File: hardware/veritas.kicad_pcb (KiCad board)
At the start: 2 copper layers, 43 parts, among them J1 ~{USB_BOOT}, J2 USB_C_Receptacle_USB2.0, J3 VIDEO, J4 VIDEO, J5 SYNC, J6 CONTROLLER_PORT, J7 CON_RESET, Q1 LMBT3946DW1T1G, U1 W25Q128JVSIQ, U2 NCP1117ST33T3G, U3 RP2040, U4 LM1881, Y1 12MHz

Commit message: Finished first hardware prototype.
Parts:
- added C17: 0.1uF, Capacitor_SMD:C_0603_1608Metric_Pad1.08x0.95mm_HandSolder, F.Cu at (154.7, 79.9)
- added C19: 0.1uF, Capacitor_SMD:C_0603_1608Metric_Pad1.08x0.95mm_HandSolder, F.Cu at (141.9, 111.8)
- added C22: 0.1uF, Capacitor_SMD:C_0603_1608Metric_Pad1.08x0.95mm_HandSolder, F.Cu at (170.2, 120.1)
- added C23: 0.1uF, Capacitor_SMD:C_0603_1608Metric_Pad1.08x0.95mm_HandSolder, F.Cu at (153.4, 115.2)
- added J11: DEBUG, Connector_PinHeader_2.54mm:PinHeader_1x06_P2.54mm_Horizontal, F.Cu at (174.4, 120.9)
- added J2: DISPLAY0, Connector_PinHeader_2.54mm:PinHeader_1x05_P2.54mm_Horizontal, F.Cu at (156.3, 70.1)
- added J3: DISPLAY1, Connector_PinHeader_2.54mm:PinHeader_1x05_P2.54mm_Horizontal, F.Cu at (141.9, 70.1)
- added J4: DISPLAY2, Connector_PinHeader_2.54mm:PinHeader_1x05_P2.54mm_Horizontal, F.Cu at (127.4, 70.1)
- added J5: DISPLAY3, Connector_PinHeader_2.54mm:PinHeader_1x05_P2.54mm_Horizontal, F.Cu at (112.9, 70.1)
- added JP3: DJ-, Jumper:SolderJumper-3_P1.3mm_Open_RoundedPad1.0x1.5mm_NumberLabels, F.Cu at (173.9, 103.2)
- added JP4: DJ+, Jumper:SolderJumper-3_P1.3mm_Open_RoundedPad1.0x1.5mm_NumberLabels, F.Cu at (173.9, 98.4)
- added JP5: SolderJumper_2_Open, Jumper:SolderJumper-2_P1.3mm_Open_TrianglePad1.0x1.5mm, B.Cu at (162.0, 111.9)
- added JP6: SolderJumper_2_Open, Jumper:SolderJumper-2_P1.3mm_Open_TrianglePad1.0x1.5mm, B.Cu at (162.0, 109.7)
- added JP7: SolderJumper_2_Open, Jumper:SolderJumper-2_P1.3mm_Open_TrianglePad1.0x1.5mm, B.Cu at (177.2, 120.2)
- added Q2: 2N7002K, Package_TO_SOT_SMD:SOT-23_Handsoldering, F.Cu at (124.7, 121.5)
- added R10: 10K, Resistor_SMD:R_0603_1608Metric_Pad0.98x0.95mm_HandSolder, F.Cu at (124.7, 117.9)
- added R12: 10K, Resistor_SMD:R_0603_1608Metric_Pad0.98x0.95mm_HandSolder, F.Cu at (123.8, 125.1)
- added R3: 1K, Resistor_SMD:R_0603_1608Metric_Pad0.98x0.95mm_HandSolder, F.Cu at (132.5, 93.3)
- added REF**: JLC_ToolingHole, veritas:JLC_ToolingHole, F.Cu at (183.1, 61.3)
- added REF**: JLC_ToolingHole, veritas:JLC_ToolingHole, F.Cu at (111.1, 63.2)
- added REF**: JLC_ToolingHole, veritas:JLC_ToolingHole, F.Cu at (113.0, 133.1)
- added SW1: ~{BOOT_SEL}, Button_Switch_SMD:SW_SPST_PTS645, F.Cu at (179.6, 86.1)
- added U4: MCP2221A, Package_DIP:DIP-14_W7.62mm, F.Cu at (157.1, 80.5)
- added U6: TXS0108EPW, Package_SO:TSSOP-20_4.4x6.5mm_P0.65mm, F.Cu at (159.0, 113.4)
- added U7: TXS0108EPW, Package_SO:TSSOP-20_4.4x6.5mm_P0.65mm, F.Cu at (147.6, 113.4)
- added U8: TXS0108EPW, Package_SO:TSSOP-20_4.4x6.5mm_P0.65mm, F.Cu at (136.1, 113.4)
- J1: value ~{USB_BOOT} -> DISPLAY_PWR; footprint Connector_PinHeader_2.54mm:PinHeader_1x02_P2.54mm_Vertical -> Connector_BarrelJack:BarrelJack_Horizontal
- J7: renamed from J2; value USB_C_Receptacle_USB2.0 -> USB2.0_C; footprint veritas:2171790001 -> veritas:TYPE-C-31-M-12
- Q1: footprint Package_TO_SOT_SMD:SOT-363_SC-70-6 -> Package_TO_SOT_SMD:SOT-363_SC-70-6_Handsoldering
- moved C2 74.6 mm to (131.7, 96.5), turned to 180 degrees
- moved J7 63.2 mm to (183.0, 100.8), turned to 90 degrees
- moved C7 62.8 mm to (172.7, 117.9)
- moved J1 61.7 mm to (171.8, 67.4), turned to 180 degrees
- moved R9 61.5 mm to (180.2, 94.7), turned to 0 degrees
- moved C4 59.8 mm to (146.4, 97.5)
- moved R8 59.6 mm to (180.2, 107.0), turned to 0 degrees
- moved C5 56.6 mm to (137.8, 100.7), turned to -90 degrees
- moved JP1 55.9 mm to (127.9, 81.2)
- moved R4 55.9 mm to (127.9, 79.2)
- moved C1 54.2 mm to (131.7, 95.0), turned to 180 degrees
- moved R5 52.8 mm to (124.5, 79.2), turned to 0 degrees
- moved C12 50.7 mm to (138.3, 86.4), turned to 90 degrees
- moved C3 50.5 mm to (142.6, 99.0), turned to -90 degrees
- moved C6 49.4 mm to (146.4, 99.1)
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- renumbered C17 to C18, C18 to C20, C19 to C21, J5 to J10, J6 to J12, J7 to J6, J3 to J8, J4 to J9, R9 to R11, R7 to R4, R8 to R5, R3 to R6, R6 to R7, R4 to R8, R5 to R9, U4 to U5
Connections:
- net ALT_CLK renamed ALT_CLK_B
- J1 pad 1: Net-(J1-Pad1) -> /LED_5V
- J12 pad 1: unconnected-(J6-Pad1) -> CP_1
- J12 pad 10: VBUS -> +3V3
- J12 pad 11: unconnected-(J6-Pad11) -> CP_11
- J12 pad 12: unconnected-(J6-Pad12) -> CP_12
- J12 pad 13: unconnected-(J6-Pad13) -> CP_13
- J12 pad 14: unconnected-(J6-Pad14) -> CP_14
- J12 pad 15: unconnected-(J6-Pad15) -> CP_15
- J12 pad 16: unconnected-(J6-Pad16) -> CP_16
- J12 pad 17: unconnected-(J6-Pad17) -> CP_17
- J12 pad 18: unconnected-(J6-Pad18) -> CP_18
- J12 pad 19: +3V3 -> VBUS
- J12 pad 2: unconnected-(J6-Pad2) -> CP_2
- J12 pad 20: unconnected-(J6-Pad20) -> CP_20
- J12 pad 21: unconnected-(J6-Pad21) -> CP_21
- J12 pad 22: unconnected-(J6-Pad22) -> CP_22
- J12 pad 23: unconnected-(J6-Pad23) -> CP_23
- J12 pad 24: unconnected-(J6-Pad24) -> CP_24
- J12 pad 25: unconnected-(J6-Pad25) -> CP_25
- J12 pad 3: unconnected-(J6-Pad3) -> CP_3
- J12 pad 4: unconnected-(J6-Pad4) -> CP_4
- J12 pad 5: unconnected-(J6-Pad5) -> CP_5
- J12 pad 6: unconnected-(J6-Pad6) -> CP_6
- J12 pad 7: unconnected-(J6-Pad7) -> CP_7
- J12 pad 8: unconnected-(J6-Pad8) -> CP_8
- J6 pad 2: /RESET_HI -> /RESET_LO
- J6 pad 3: /RESET_LO -> /RESET_HI
- J7 pad A6: /D+ -> /PORTD+
- J7 pad A7: /D- -> /PORTD-
- J7 pad B6: /D+ -> /PORTD+
- J7 pad B7: /D- -> /PORTD-
- Q1 pad 6: VDD -> CP_20
- R1 pad 1: Net-(J1-Pad1) -> Net-(R1-Pad1)
- U3 pad 11: unconnected-(U3-Pad11) -> BRIDGE_RX
- U3 pad 12: unconnected-(U3-Pad12) -> BRIDGE_TX
- U3 pad 13: unconnected-(U3-Pad13) -> CON_RESET
- U3 pad 14: unconnected-(U3-Pad14) -> ALT_CLK_A
- U3 pad 15: unconnected-(U3-Pad15) -> CNT_0
- U3 pad 16: unconnected-(U3-Pad16) -> CNT_1
- U3 pad 17: unconnected-(U3-Pad17) -> CNT_2
- U3 pad 18: unconnected-(U3-Pad18) -> CNT_3
- U3 pad 19: unconnected-(U3-Pad19) -> GND
- U3 pad 2: unconnected-(U3-Pad2) -> CNT_17
- U3 pad 21: Net-(C14-Pad2) -> Net-(R3-Pad2)
- U3 pad 24: unconnected-(U3-Pad24) -> SWCLK
- U3 pad 25: unconnected-(U3-Pad25) -> SWD
- U3 pad 26: unconnected-(U3-Pad26) -> +3V3
- U3 pad 27: unconnected-(U3-Pad27) -> CNT_4
- U3 pad 28: unconnected-(U3-Pad28) -> CNT_5
- U3 pad 29: unconnected-(U3-Pad29) -> CNT_6
- U3 pad 3: unconnected-(U3-Pad3) -> CNT_18
- U3 pad 30: unconnected-(U3-Pad30) -> CNT_7
- U3 pad 31: unconnected-(U3-Pad31) -> CNT_8
- U3 pad 32: unconnected-(U3-Pad32) -> CNT_9
- U3 pad 34: unconnected-(U3-Pad34) -> CNT_10
- U3 pad 35: unconnected-(U3-Pad35) -> CNT_11
- U3 pad 36: unconnected-(U3-Pad36) -> CNT_12
- U3 pad 37: unconnected-(U3-Pad37) -> CNT_13
- U3 pad 38: unconnected-(U3-Pad38) -> CNT_14
- U3 pad 39: unconnected-(U3-Pad39) -> CNT_15
- U3 pad 4: unconnected-(U3-Pad4) -> DISPLAY_STROBE0
- U3 pad 40: unconnected-(U3-Pad40) -> CNT_16
- U3 pad 41: unconnected-(U3-Pad41) -> DETECT
- U3 pad 5: unconnected-(U3-Pad5) -> DISPLAY_STROBE1
- U3 pad 6: unconnected-(U3-Pad6) -> DISPLAY_STROBE2
- U3 pad 7: unconnected-(U3-Pad7) -> DISPLAY_STROBE3
- U3 pad 8: unconnected-(U3-Pad8) -> DISPLAY_SER
- U3 pad 9: unconnected-(U3-Pad9) -> DISPLAY_CLK
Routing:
- net +3V3: track 15.4 -> 225.7 mm, vias 0 -> 4
- net SWCLK: track 0.00 -> 132.0 mm, vias 0 -> 2
- net SWD: track 0.00 -> 129.2 mm, vias 0 -> 2
- net GND: track 16.1 -> 135.4 mm, vias 6 -> 28
- net DISPLAY_CLK: track 0.00 -> 116.8 mm
- net DISPLAY_SER: track 0.00 -> 111.7 mm, vias 0 -> 1
- net VBUS: track 2.54 -> 101.3 mm, vias 0 -> 3
- net CP_20: track 0.00 -> 97.9 mm, vias 0 -> 1
- net /LED_5V: track 0.00 -> 80.1 mm
- net CNT_17: track 0.00 -> 70.3 mm, vias 0 -> 3
- net CNT_18: track 0.00 -> 65.2 mm, vias 0 -> 3
- net ALT_CLK_A: track 0.00 -> 51.3 mm, vias 0 -> 2
- net DISPLAY_STROBE3: track 0.00 -> 40.0 mm
- net DISPLAY_STROBE0: track 0.00 -> 36.0 mm
- net Net-(R1-Pad1): track 0.00 -> 35.1 mm
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- added copper zone on F.Cu, net +1V1
- added copper zone on F.Cu, net +3V3
- added copper zone on B.Cu, net GND
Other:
- board outline added: 76.1 x 77.3 mm
- board text added: "5V"
- board text added: "ALT_CLK"
- board text added: "CVIN"
- board text added: "DEBUG_RX"
- board text added: "DEBUG_TX"
- board text added: "GND"
- board text added: "JLCJLCJLCJLC"
- board text added: "OEOUT"
- board text added: "RESET_HI"
- board text added: "RESET_LO"
- board text added: "SWCLK"
- board text added: "SWD"
- board text added: "VeriTAS by Bigbass Licensed under CERN-OHL-W-2.0 2022-08-15"

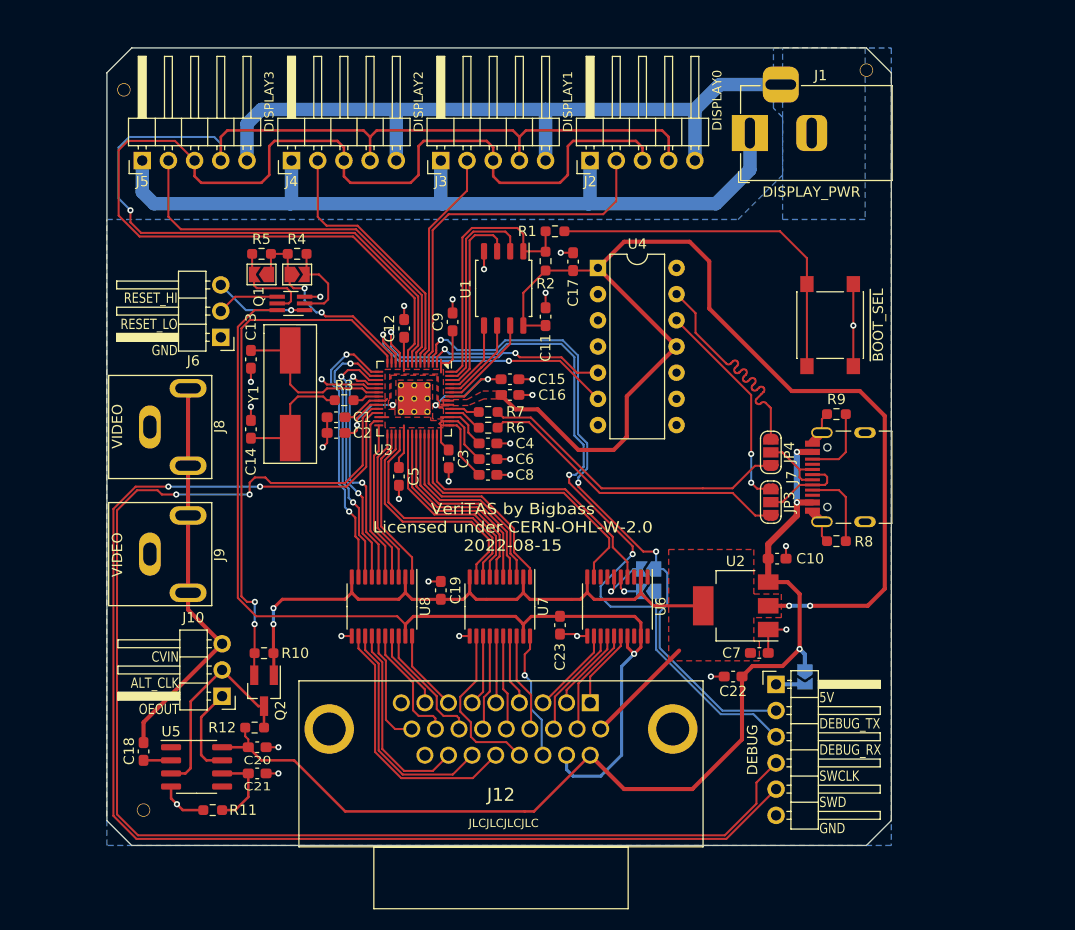
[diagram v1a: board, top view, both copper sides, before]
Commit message: Completed new PCB revision. Includes different voltage translation and removal of unnecessary parts.
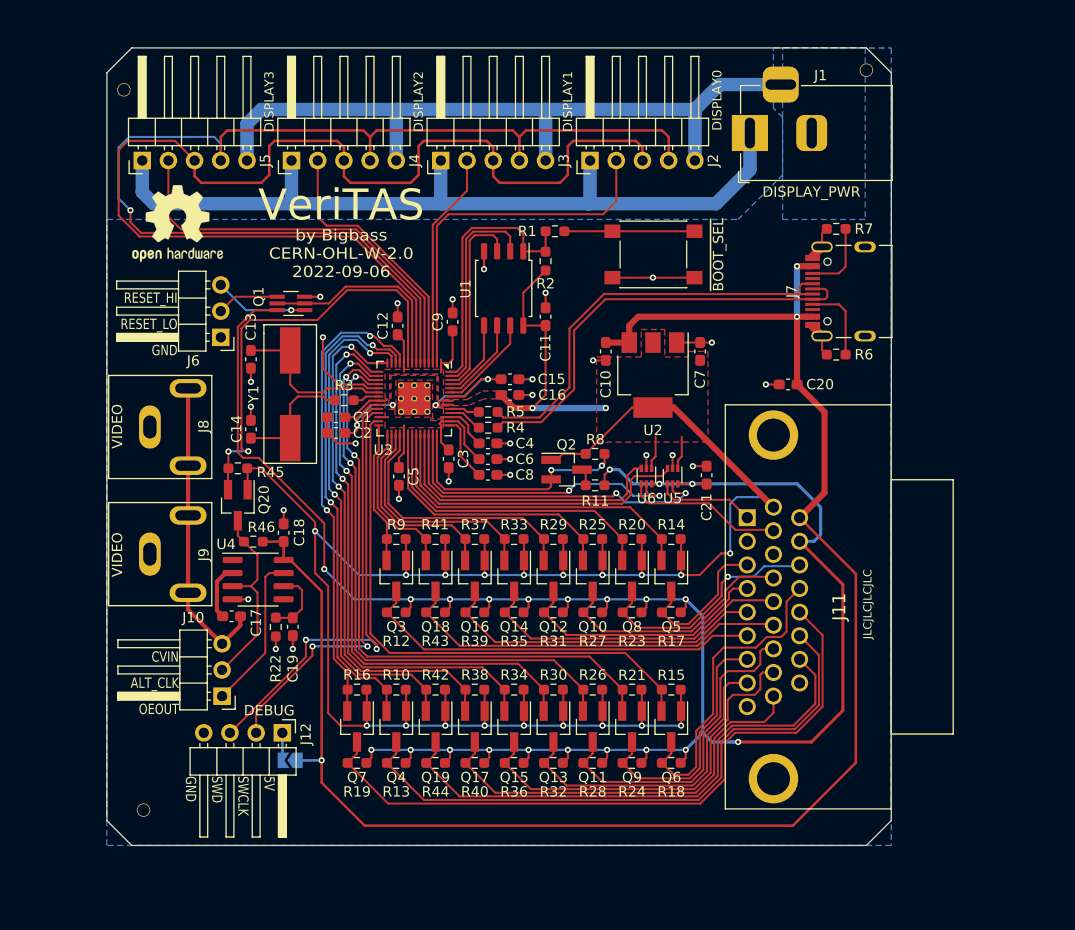
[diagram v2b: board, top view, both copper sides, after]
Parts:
- removed the C17 at (154.7, 79.9)
- removed the C19 at (141.9, 111.8)
- removed the JP1 at (127.9, 81.2)
- removed JP2, JP5, JP6: SolderJumper_2_Open, Jumper:SolderJumper-2_P1.3mm_Open_TrianglePad1.0x1.5mm
- removed JP3: DJ-, Jumper:SolderJumper-3_P1.3mm_Open_RoundedPad1.0x1.5mm_NumberLabels
- removed JP4: DJ+, Jumper:SolderJumper-3_P1.3mm_Open_RoundedPad1.0x1.5mm_NumberLabels
- removed the R4 at (127.9, 79.2)
- removed the R5 at (124.5, 79.2)
- removed the U4 at (157.1, 80.5)
- removed U7, U8: TXS0108EPW, Package_SO:TSSOP-20_4.4x6.5mm_P0.65mm
- added Q10: 2N7002K, Package_TO_SOT_SMD:SOT-23_Handsoldering, F.Cu at (156.6, 110.4)
- added Q11: 2N7002K, Package_TO_SOT_SMD:SOT-23_Handsoldering, F.Cu at (156.6, 125.0)
- added Q12: 2N7002K, Package_TO_SOT_SMD:SOT-23_Handsoldering, F.Cu at (152.8, 110.4)
- added Q13: 2N7002K, Package_TO_SOT_SMD:SOT-23_Handsoldering, F.Cu at (152.8, 125.0)
- added Q14: 2N7002K, Package_TO_SOT_SMD:SOT-23_Handsoldering, F.Cu at (149.0, 110.4)
- added Q15: 2N7002K, Package_TO_SOT_SMD:SOT-23_Handsoldering, F.Cu at (149.0, 125.0)
- added Q16: 2N7002K, Package_TO_SOT_SMD:SOT-23_Handsoldering, F.Cu at (145.2, 110.4)
- added Q17: 2N7002K, Package_TO_SOT_SMD:SOT-23_Handsoldering, F.Cu at (145.2, 125.0)
- added Q18: 2N7002K, Package_TO_SOT_SMD:SOT-23_Handsoldering, F.Cu at (141.4, 110.4)
- added Q19: 2N7002K, Package_TO_SOT_SMD:SOT-23_Handsoldering, F.Cu at (141.4, 125.0)
- added Q2: 2N7002K, Package_TO_SOT_SMD:SOT-23_Handsoldering, F.Cu at (154.1, 100.1)
- added Q3: 2N7002K, Package_TO_SOT_SMD:SOT-23_Handsoldering, F.Cu at (137.5, 110.4)
- added Q4: 2N7002K, Package_TO_SOT_SMD:SOT-23_Handsoldering, F.Cu at (137.5, 125.0)
- added Q5: 2N7002K, Package_TO_SOT_SMD:SOT-23_Handsoldering, F.Cu at (164.2, 110.4)
- added Q6: 2N7002K, Package_TO_SOT_SMD:SOT-23_Handsoldering, F.Cu at (164.2, 125.0)
- added Q7: 2N7002K, Package_TO_SOT_SMD:SOT-23_Handsoldering, F.Cu at (133.7, 125.0)
- added Q8: 2N7002K, Package_TO_SOT_SMD:SOT-23_Handsoldering, F.Cu at (160.4, 110.4)
- added Q9: 2N7002K, Package_TO_SOT_SMD:SOT-23_Handsoldering, F.Cu at (160.4, 125.0)
- added R10: 10K, Resistor_SMD:R_0603_1608Metric_Pad0.98x0.95mm_HandSolder, F.Cu at (137.5, 121.4)
- added R11: 10K, Resistor_SMD:R_0603_1608Metric_Pad0.98x0.95mm_HandSolder, F.Cu at (156.8, 101.6)
- added R13: 10K, Resistor_SMD:R_0603_1608Metric_Pad0.98x0.95mm_HandSolder, F.Cu at (137.5, 128.5)
- added R14: 10K, Resistor_SMD:R_0603_1608Metric_Pad0.98x0.95mm_HandSolder, F.Cu at (164.2, 106.8)
- added R15: 10K, Resistor_SMD:R_0603_1608Metric_Pad0.98x0.95mm_HandSolder, F.Cu at (164.2, 121.4)
- added R16: 10K, Resistor_SMD:R_0603_1608Metric_Pad0.98x0.95mm_HandSolder, F.Cu at (133.7, 121.4)
- added R17: 10K, Resistor_SMD:R_0603_1608Metric_Pad0.98x0.95mm_HandSolder, F.Cu at (164.2, 113.9)
- added R18: 10K, Resistor_SMD:R_0603_1608Metric_Pad0.98x0.95mm_HandSolder, F.Cu at (164.2, 128.5)
- added R19: 10K, Resistor_SMD:R_0603_1608Metric_Pad0.98x0.95mm_HandSolder, F.Cu at (133.7, 128.5)
- added R20: 10K, Resistor_SMD:R_0603_1608Metric_Pad0.98x0.95mm_HandSolder, F.Cu at (160.4, 106.8)
- added R21: 10K, Resistor_SMD:R_0603_1608Metric_Pad0.98x0.95mm_HandSolder, F.Cu at (160.4, 121.4)
- added R23: 10K, Resistor_SMD:R_0603_1608Metric_Pad0.98x0.95mm_HandSolder, F.Cu at (160.4, 113.9)
- added R24: 10K, Resistor_SMD:R_0603_1608Metric_Pad0.98x0.95mm_HandSolder, F.Cu at (160.4, 128.5)
- added R25: 10K, Resistor_SMD:R_0603_1608Metric_Pad0.98x0.95mm_HandSolder, F.Cu at (156.6, 106.8)
- added R26: 10K, Resistor_SMD:R_0603_1608Metric_Pad0.98x0.95mm_HandSolder, F.Cu at (156.6, 121.4)
- added R27: 10K, Resistor_SMD:R_0603_1608Metric_Pad0.98x0.95mm_HandSolder, F.Cu at (156.6, 113.9)
- added R28: 10K, Resistor_SMD:R_0603_1608Metric_Pad0.98x0.95mm_HandSolder, F.Cu at (156.6, 128.5)
- added R29: 10K, Resistor_SMD:R_0603_1608Metric_Pad0.98x0.95mm_HandSolder, F.Cu at (152.8, 106.8)
- added R30: 10K, Resistor_SMD:R_0603_1608Metric_Pad0.98x0.95mm_HandSolder, F.Cu at (152.8, 121.4)
- added R31: 10K, Resistor_SMD:R_0603_1608Metric_Pad0.98x0.95mm_HandSolder, F.Cu at (152.8, 113.9)
- added R32: 10K, Resistor_SMD:R_0603_1608Metric_Pad0.98x0.95mm_HandSolder, F.Cu at (152.8, 128.5)
- added R33: 10K, Resistor_SMD:R_0603_1608Metric_Pad0.98x0.95mm_HandSolder, F.Cu at (149.0, 106.8)
- added R34: 10K, Resistor_SMD:R_0603_1608Metric_Pad0.98x0.95mm_HandSolder, F.Cu at (149.0, 121.4)
- added R35: 10K, Resistor_SMD:R_0603_1608Metric_Pad0.98x0.95mm_HandSolder, F.Cu at (149.0, 113.9)
- added R36: 10K, Resistor_SMD:R_0603_1608Metric_Pad0.98x0.95mm_HandSolder, F.Cu at (149.0, 128.5)
- added R37: 10K, Resistor_SMD:R_0603_1608Metric_Pad0.98x0.95mm_HandSolder, F.Cu at (145.2, 106.8)
- added R38: 10K, Resistor_SMD:R_0603_1608Metric_Pad0.98x0.95mm_HandSolder, F.Cu at (145.2, 121.4)
- added R39: 10K, Resistor_SMD:R_0603_1608Metric_Pad0.98x0.95mm_HandSolder, F.Cu at (145.2, 113.9)
- added R40: 10K, Resistor_SMD:R_0603_1608Metric_Pad0.98x0.95mm_HandSolder, F.Cu at (145.2, 128.5)
- added R41: 10K, Resistor_SMD:R_0603_1608Metric_Pad0.98x0.95mm_HandSolder, F.Cu at (141.4, 106.8)
- added R42: 10K, Resistor_SMD:R_0603_1608Metric_Pad0.98x0.95mm_HandSolder, F.Cu at (141.4, 121.4)
- added R43: 10K, Resistor_SMD:R_0603_1608Metric_Pad0.98x0.95mm_HandSolder, F.Cu at (141.4, 113.9)
- added R44: 10K, Resistor_SMD:R_0603_1608Metric_Pad0.98x0.95mm_HandSolder, F.Cu at (141.4, 128.5)
- added R46: 10K, Resistor_SMD:R_0603_1608Metric_Pad0.98x0.95mm_HandSolder, F.Cu at (123.7, 107.1)
- added R8: 10K, Resistor_SMD:R_0603_1608Metric_Pad0.98x0.95mm_HandSolder, F.Cu at (156.8, 98.6)
- added R9: 10K, Resistor_SMD:R_0603_1608Metric_Pad0.98x0.95mm_HandSolder, F.Cu at (137.5, 106.8)
- added REF**: OSHW-Logo2_9.8x8mm_SilkScreen, Symbol:OSHW-Logo2_9.8x8mm_SilkScreen, F.Cu at (116.3, 76.2)
- added U5: SN74LVC1T45DRL, Package_TO_SOT_SMD:SOT-563, F.Cu at (164.3, 100.7)
- J12: renamed from J11; footprint Connector_PinHeader_2.54mm:PinHeader_1x06_P2.54mm_Horizontal -> Connector_PinHeader_2.54mm:PinHeader_1x04_P2.54mm_Horizontal
- U6: value TXS0108EPW -> SN74LVC1T45DRL; footprint Package_SO:TSSOP-20_4.4x6.5mm_P0.65mm -> Package_TO_SOT_SMD:SOT-563
- moved JP1 50.6 mm to (127.3, 128.3), turned to 180 degrees
- moved J12 48.1 mm to (126.5, 125.6), turned to -90 degrees
- moved C7 29.8 mm to (167.0, 88.6), turned to 90 degrees
- moved C20 28.8 mm to (175.5, 91.8)
- moved C10 26.1 mm to (157.9, 88.6), turned to -90 degrees
- moved U2 23.8 mm to (162.4, 90.9), turned to -90 degrees
- moved J11 23.5 mm to (171.6, 104.7), turned to 90 degrees
- moved C18 21.0 mm to (126.6, 106.2), turned to -90 degrees
- moved C21 20.3 mm to (167.6, 100.6), turned to 90 degrees
- moved U4 19.1 mm to (124.1, 110.7)
- moved R22 18.8 mm to (125.9, 115.3), turned to -90 degrees
- moved SW1 18.5 mm to (162.5, 79.2), turned to 180 degrees
- moved Q20 18.2 mm to (122.2, 103.5)
- moved R45 18.1 mm to (122.2, 99.9)
- moved R6 18.1 mm to (180.2, 88.9)
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- renumbered C18 to C17, C20 to C18, C21 to C19, C22 to C20, C23 to C21, J12 to J11, JP7 to JP1, Q2 to Q20, R11 to R22, R6 to R4, R10 to R45, R7 to R5, R8 to R6, R9 to R7, U5 to U4
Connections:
- C21 pad 1: CP_20 -> SYSTEM_PWR
- J11 pad 20: CP_20 -> SYSTEM_PWR
- J12 pad 2: CNT_18 -> SWCLK
- J12 pad 3: CNT_17 -> SWD
- J12 pad 4: SWCLK -> GND
- J7 pad A6: /PORTD+ -> /D+
- J7 pad A7: /PORTD- -> /D-
- J7 pad B6: /PORTD+ -> /D+
- J7 pad B7: /PORTD- -> /D-
- Q1 pad 2: Net-(JP1-Pad2) -> CON_RESET
- Q1 pad 5: Net-(JP2-Pad2) -> CON_RESET
- Q1 pad 6: CP_20 -> SYSTEM_PWR
- R12 pad 1: ALT_CLK_B -> CP_6
- R12 pad 2: VBUS -> SYSTEM_PWR
- U3 pad 11: BRIDGE_RX -> CNT_0
- U3 pad 12: BRIDGE_TX -> CNT_1
- U3 pad 13: CON_RESET -> CNT_2
- U3 pad 14: ALT_CLK_A -> CNT_3
- U3 pad 15: CNT_0 -> CNT_4
- U3 pad 16: CNT_1 -> CNT_5
- U3 pad 17: CNT_2 -> CNT_6
- U3 pad 18: CNT_3 -> CNT_7
- U3 pad 2: CNT_17 -> DISPLAY_STROBE0
- U3 pad 27: CNT_4 -> CNT_8
- U3 pad 28: CNT_5 -> CNT_9
- U3 pad 29: CNT_6 -> CNT_10
- U3 pad 3: CNT_18 -> DISPLAY_STROBE1
- U3 pad 30: CNT_7 -> CNT_11
- U3 pad 31: CNT_8 -> CNT_12
- U3 pad 32: CNT_9 -> CNT_13
- U3 pad 34: CNT_10 -> CNT_14
- U3 pad 35: CNT_11 -> CNT_15
- U3 pad 36: CNT_12 -> CNT_16
- U3 pad 37: CNT_13 -> CNT_17
- U3 pad 38: CNT_14 -> CNT_18
- U3 pad 39: CNT_15 -> CNT_17_DIR
- U3 pad 4: DISPLAY_STROBE0 -> DISPLAY_STROBE2
- U3 pad 40: CNT_16 -> CNT_18_DIR
- U3 pad 5: DISPLAY_STROBE1 -> DISPLAY_STROBE3
- U3 pad 6: DISPLAY_STROBE2 -> DISPLAY_SER
- U3 pad 7: DISPLAY_STROBE3 -> DISPLAY_CLK
- U3 pad 8: DISPLAY_SER -> CON_RESET
- U3 pad 9: DISPLAY_CLK -> ALT_CLK_A
- U6 pad 1: unconnected-(U6-Pad1) -> +3V3
- U6 pad 2: +3V3 -> GND
- U6 pad 3: unconnected-(U6-Pad3) -> CNT_18
- U6 pad 4: DETECT -> CP_11
- U6 pad 5: Net-(JP5-Pad2) -> CNT_18_DIR
- U6 pad 6: Net-(JP6-Pad2) -> SYSTEM_PWR
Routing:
- net SYSTEM_PWR: track 0.00 -> 205.7 mm, vias 0 -> 22
- net CP_20: track 97.9 -> 0.00 mm, vias 1 -> 0
- net SWCLK: track 132.0 -> 40.3 mm
- net SWD: track 129.2 -> 43.7 mm
- net VBUS: track 101.3 -> 161.7 mm
- net +3V3: track 225.7 -> 275.7 mm, vias 4 -> 21
- net CNT_7: track 15.5 -> 59.0 mm, vias 0 -> 2
- net CNT_6: track 15.1 -> 56.6 mm, vias 0 -> 2
- net CP_23: track 25.6 -> 66.1 mm
- net CNT_5: track 15.6 -> 54.3 mm, vias 0 -> 2
- net CNT_17: track 70.3 -> 32.0 mm, vias 3 -> 0
- net CP_24: track 22.4 -> 59.2 mm
- net CNT_18: track 65.2 -> 28.8 mm, vias 3 -> 0
- net CNT_4: track 16.3 -> 52.3 mm, vias 0 -> 2
- net CNT_17_DIR: track 0.00 -> 33.1 mm, vias 0 -> 2
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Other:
- board text added: "VeriTAS"
- board text added: "by Bigbass CERN-OHL-W-2.0 2022-09-06"
- board text removed: "DEBUG_RX"
- board text removed: "DEBUG_TX"
- board text removed: "VeriTAS by Bigbass Licensed under CERN-OHL-W-2.0 2022-08-15"
